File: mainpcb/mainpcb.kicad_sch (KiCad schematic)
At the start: 38 parts

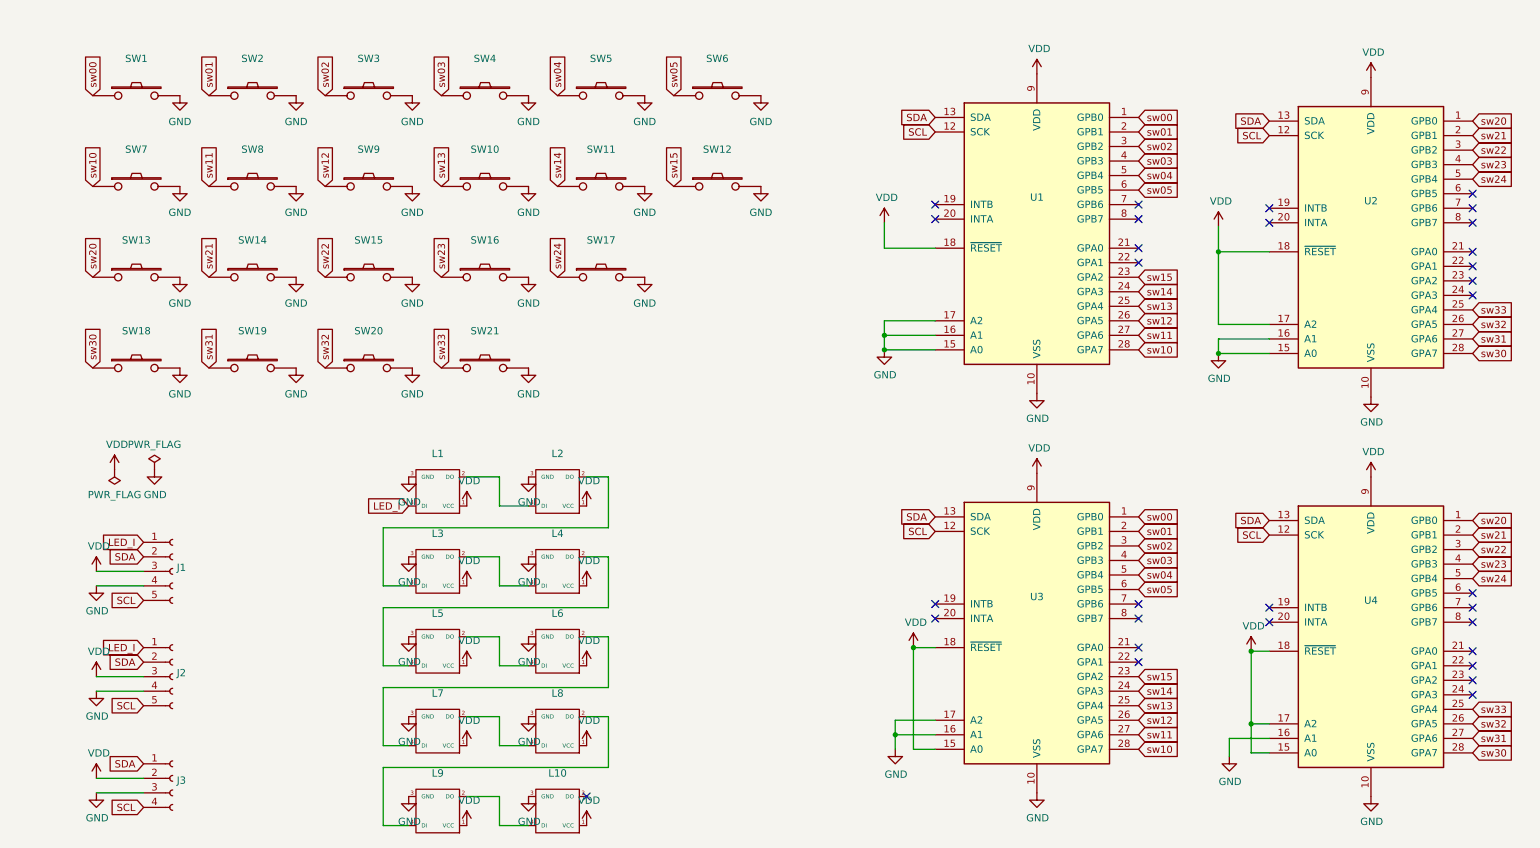
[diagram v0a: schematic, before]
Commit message: key-matrix using single mcp23017
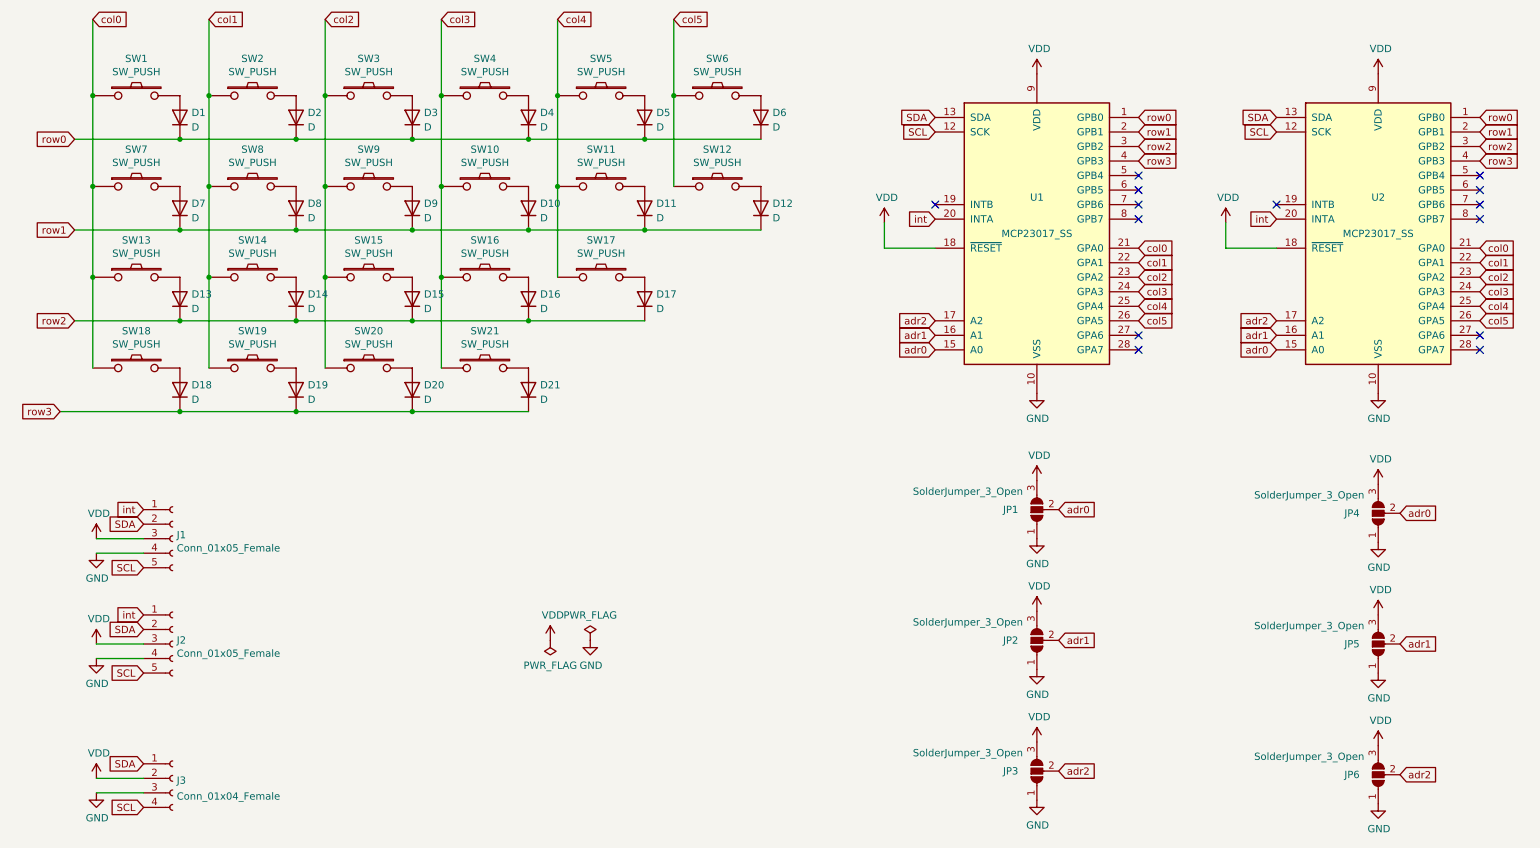
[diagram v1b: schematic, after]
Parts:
- removed L1, L10, L2, L3, L4, L5, L6, L7, L8, L9: (no value), symbol mammoth:YS-SK6812MINI
- removed U3, U4: (no value), symbol Interface_Expansion:MCP23017_SS
- added D1, D10, D11, D12, D13, D14, D15, D16, D17, D18, D19, D2, D20, D21, D3, D4, D5, D6, D7, D8, D9: D, symbol Device:D
- added JP1, JP2, JP3, JP4, JP5, JP6: SolderJumper_3_Open, symbol Jumper:SolderJumper_3_Open
- J1, J2: value (none) -> Conn_01x05_Female; footprint (none) -> mammoth:JST_ACH_BM05B-ACHSS-A-GAN-ETF_1x05-1MP_P1.20mm_Vertical
- J3: value (none) -> Conn_01x04_Female
- SW1, SW10, SW11, SW12, SW13, SW14, SW15, SW16, SW17, SW18, SW19, SW2, SW20, SW21, SW3, SW4, SW5, SW6, SW7, SW8, SW9: value (none) -> SW_PUSH; footprint (none) -> mammoth:MX_Hotswap_R_1u
- U1, U2: value (none) -> MCP23017_SS; footprint (none) -> Package_SO:SSOP-28_5.3x10.2mm_P0.65mm
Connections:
- net LED_I is gone; now on net int: J1.1 (Pin_1), J2.1 (Pin_1)
- net GND: now also JP1.1 (A), JP2.1 (A), JP3.1 (A), JP4.1 (A), JP5.1 (A), JP6.1 (A); no longer SW1.2, SW10.2, SW11.2, SW12.2, SW13.2, SW14.2, SW15.2, SW16.2, SW17.2, SW18.2, SW19.2, SW2.2, SW20.2, SW21.2, SW3.2, SW4.2, SW5.2, SW6.2, SW7.2, SW8.2, SW9.2, U1.15 (A0), U1.16 (A1), U1.17 (A2), U2.15 (A0), U2.16 (A1)
- net VDD: now also JP1.3 (B), JP2.3 (B), JP3.3 (B), JP4.3 (B), JP5.3 (B), JP6.3 (B); no longer U2.17 (A2)
- net int: now reaches U1.20 (INTA)
- net int: now also U2.20 (INTA)
- net col0: now reaches U1.21 (GPA0)
- net col0: now also SW1.1, SW13.1, SW18.1, SW7.1, U2.21 (GPA0)
- net col1: now reaches U1.22 (GPA1)
- net col1: now also SW14.1, SW19.1, SW2.1, SW8.1, U2.22 (GPA1)
- net col2: now reaches U2.23 (GPA2)
- net col2: now also SW15.1, SW20.1, SW3.1, SW9.1, U1.23 (GPA2)
- net col3: now reaches U2.24 (GPA3)
- net col3: now also SW10.1, SW16.1, SW21.1, SW4.1, U1.24 (GPA3)
- net sw00 renamed row0
- net row0: now also U2.1 (GPB0), D1.1 (K), D2.1 (K), D3.1 (K), D4.1 (K), D5.1 (K), D6.1 (K); no longer SW1.1
- net sw01 renamed row1
- net row1: now also U2.2 (GPB1), D10.1 (K), D11.1 (K), D12.1 (K), D7.1 (K), D8.1 (K), D9.1 (K); no longer SW2.1
- net sw02 renamed row2
- net row2: now also U2.3 (GPB2), D13.1 (K), D14.1 (K), D15.1 (K), D16.1 (K), D17.1 (K); no longer SW3.1
- net sw03 renamed row3
- net row3: now also U2.4 (GPB3), D18.1 (K), D19.1 (K), D20.1 (K), D21.1 (K); no longer SW4.1
- net sw04: no longer names the net of U1.5 (GPB4)
- net sw04: no longer SW5.1
- net sw05: no longer names the net of U1.6 (GPB5)
- net sw05: no longer SW6.1
- net sw10: no longer names the net of U1.28 (GPA7)
- net sw10: no longer SW7.1
- net sw11: no longer names the net of U1.27 (GPA6)
- net sw11: no longer SW8.1
- net sw12 renamed col5
- net col5: now also SW12.1, SW6.1, U2.26 (GPA5); no longer SW9.1
- net sw13 renamed col4
- net col4: now also SW11.1, SW17.1, SW5.1, U2.25 (GPA4); no longer SW10.1
- removed net sw14: SW11.1, U1.24 (GPA3)
- removed net sw15: SW12.1, U1.23 (GPA2)
- removed net sw20: SW13.1, U2.1 (GPB0)
- removed net sw21: SW14.1, U2.2 (GPB1)
- removed net sw22: SW15.1, U2.3 (GPB2)
- removed net sw23: SW16.1, U2.4 (GPB3)
- net sw24: no longer names the net of U2.5 (GPB4)
- net sw24: no longer SW17.1
- net sw30: no longer names the net of U2.28 (GPA7)
- net sw30: no longer SW18.1
- net sw31: no longer names the net of U2.27 (GPA6)
- net sw31: no longer SW19.1
- removed net sw32: SW20.1, U2.26 (GPA5)
- removed net sw33: SW21.1, U2.25 (GPA4)
- new net: D1.2 (A), SW1.2
- new net: D2.2 (A), SW2.2
- new net: D3.2 (A), SW3.2
- new net: D4.2 (A), SW4.2
- new net: D5.2 (A), SW5.2
- new net: D6.2 (A), SW6.2
- new net: D7.2 (A), SW7.2
- new net: D8.2 (A), SW8.2
- new net: D9.2 (A), SW9.2
- new net: D10.2 (A), SW10.2
- new net: D11.2 (A), SW11.2
- new net: D12.2 (A), SW12.2
- new net: D13.2 (A), SW13.2
- new net: D14.2 (A), SW14.2
- new net: D15.2 (A), SW15.2
- new net: D16.2 (A), SW16.2
- new net: D17.2 (A), SW17.2
- new net: D18.2 (A), SW18.2
- new net: D19.2 (A), SW19.2
- new net: D20.2 (A), SW20.2
- new net: D21.2 (A), SW21.2
- new net adr0: JP1.2 (C), JP4.2 (C), U1.15 (A0), U2.15 (A0)
- new net adr1: JP2.2 (C), JP5.2 (C), U1.16 (A1), U2.16 (A1)
- new net adr2: JP3.2 (C), JP6.2 (C), U1.17 (A2), U2.17 (A2)
- no-connect marks 31 -> 14
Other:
- moved on the sheet: J1, J2

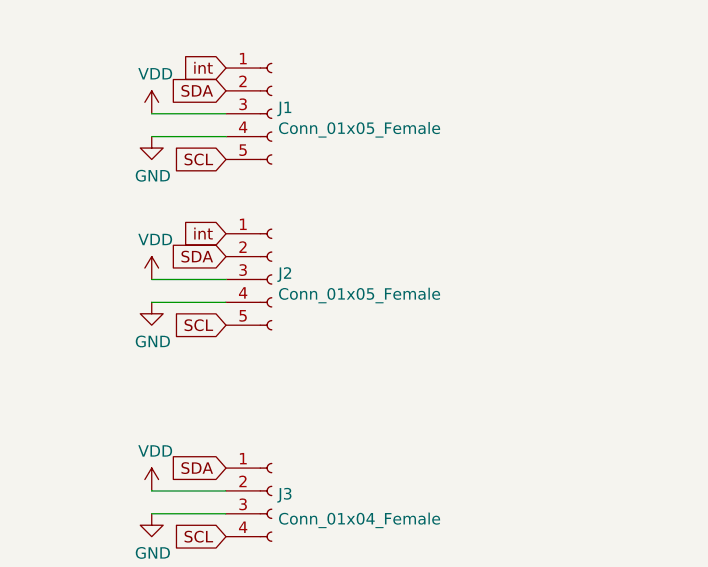
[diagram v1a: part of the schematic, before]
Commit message: fix footprint
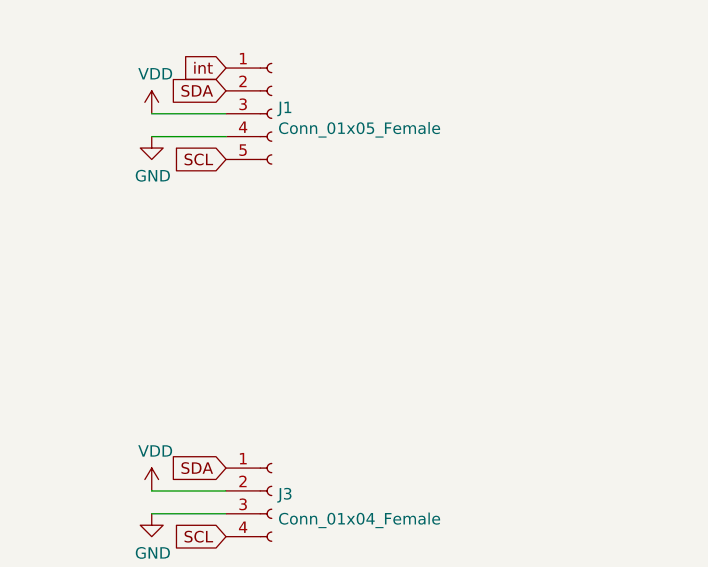
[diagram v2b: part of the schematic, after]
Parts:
- removed J2: Conn_01x05_Female, mammoth:JST_ACH_BM05B-ACHSS-A-GAN-ETF_1x05-1MP_P1.20mm_Vertical, symbol Connector:Conn_01x05_Female
- D1, D10, D11, D12, D13, D14, D15, D16, D17, D18, D19, D2, D20, D21, D3, D4, D5, D6, D7, D8, D9: footprint (none) -> mammoth:D_SOD-323_HandSoldering_rev
- J1: footprint mammoth:JST_ACH_BM05B-ACHSS-A-GAN-ETF_1x05-1MP_P1.20mm_Vertical -> (none)
- J3: footprint (none) -> Connector_PinSocket_2.54mm:PinSocket_1x04_P2.54mm_Vertical
- JP1, JP2, JP3, JP4, JP5, JP6: footprint (none) -> Jumper:SolderJumper-3_P1.3mm_Open_Pad1.0x1.5mm

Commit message: revenge 4
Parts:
- removed J3: Conn_01x04_Female, Connector_PinSocket_2.54mm:PinSocket_1x04_P2.54mm_Vertical, symbol Connector:Conn_01x04_Female
- D1, D10, D11, D12, D13, D14, D15, D16, D17, D18, D19, D2, D20, D21, D3, D4, D5, D6, D7, D8, D9: footprint mammoth:D_SOD-323_HandSoldering_rev -> (none)
- J1: footprint (none) -> mammoth:JST_ACH_BM05B-ACHSS-A-GAN-ETF_1x05-1MP_P1.20mm_Vertical_rev
